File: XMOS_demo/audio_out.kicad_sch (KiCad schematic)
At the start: 26 parts, among them J5 Conn_01x06_Socket, J6 AudioJack3_SwitchT, U7 MAX97220C

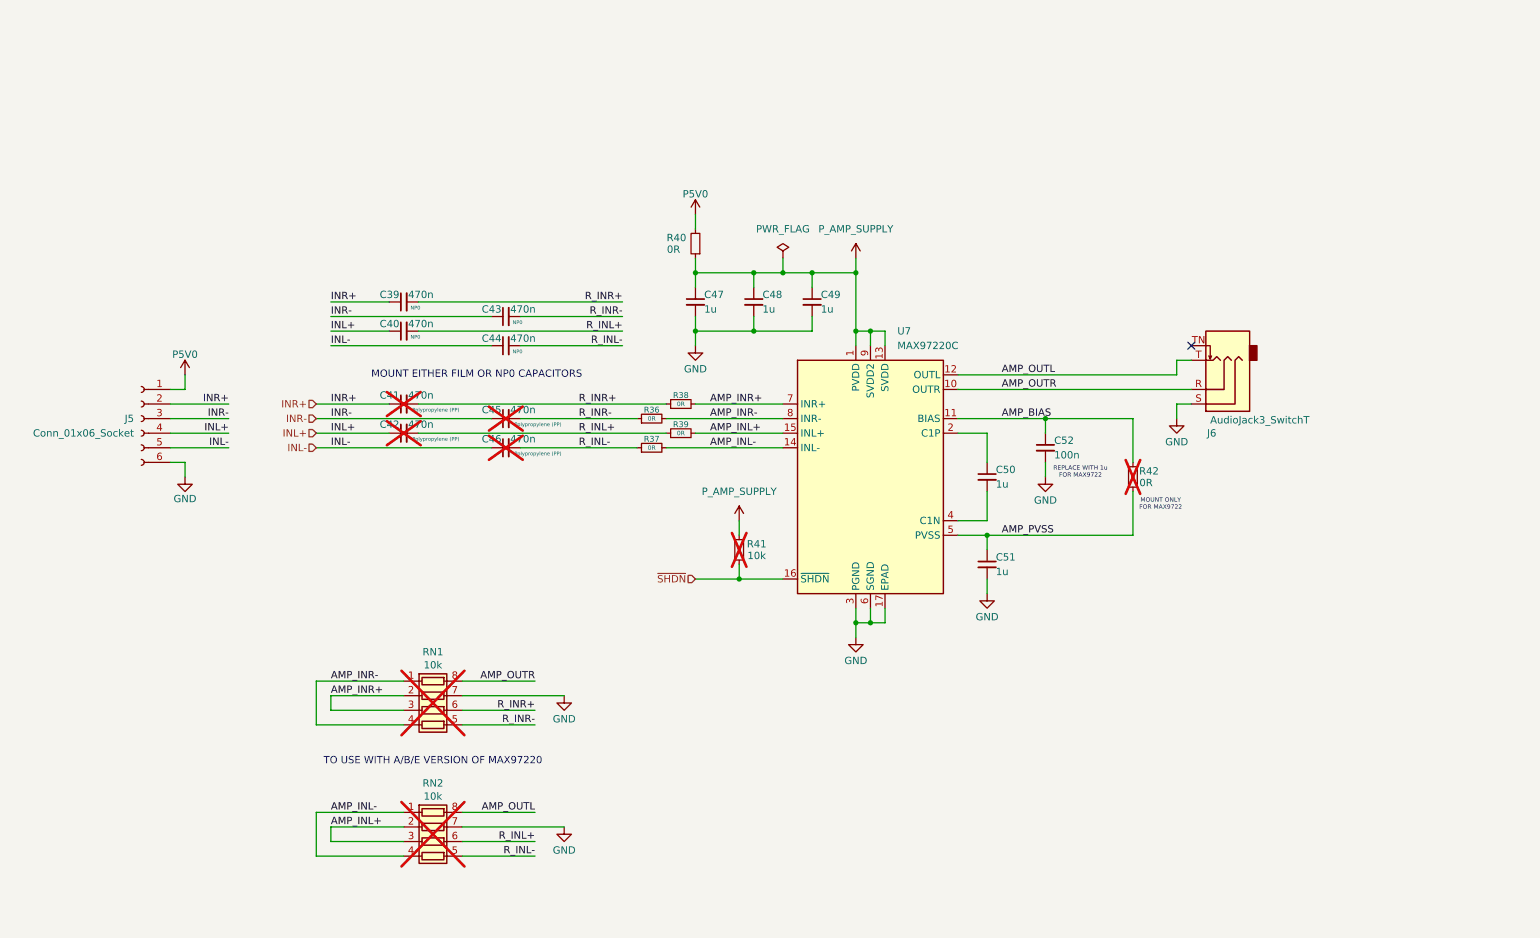
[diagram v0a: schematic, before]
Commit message: Passive lpf added to autio output
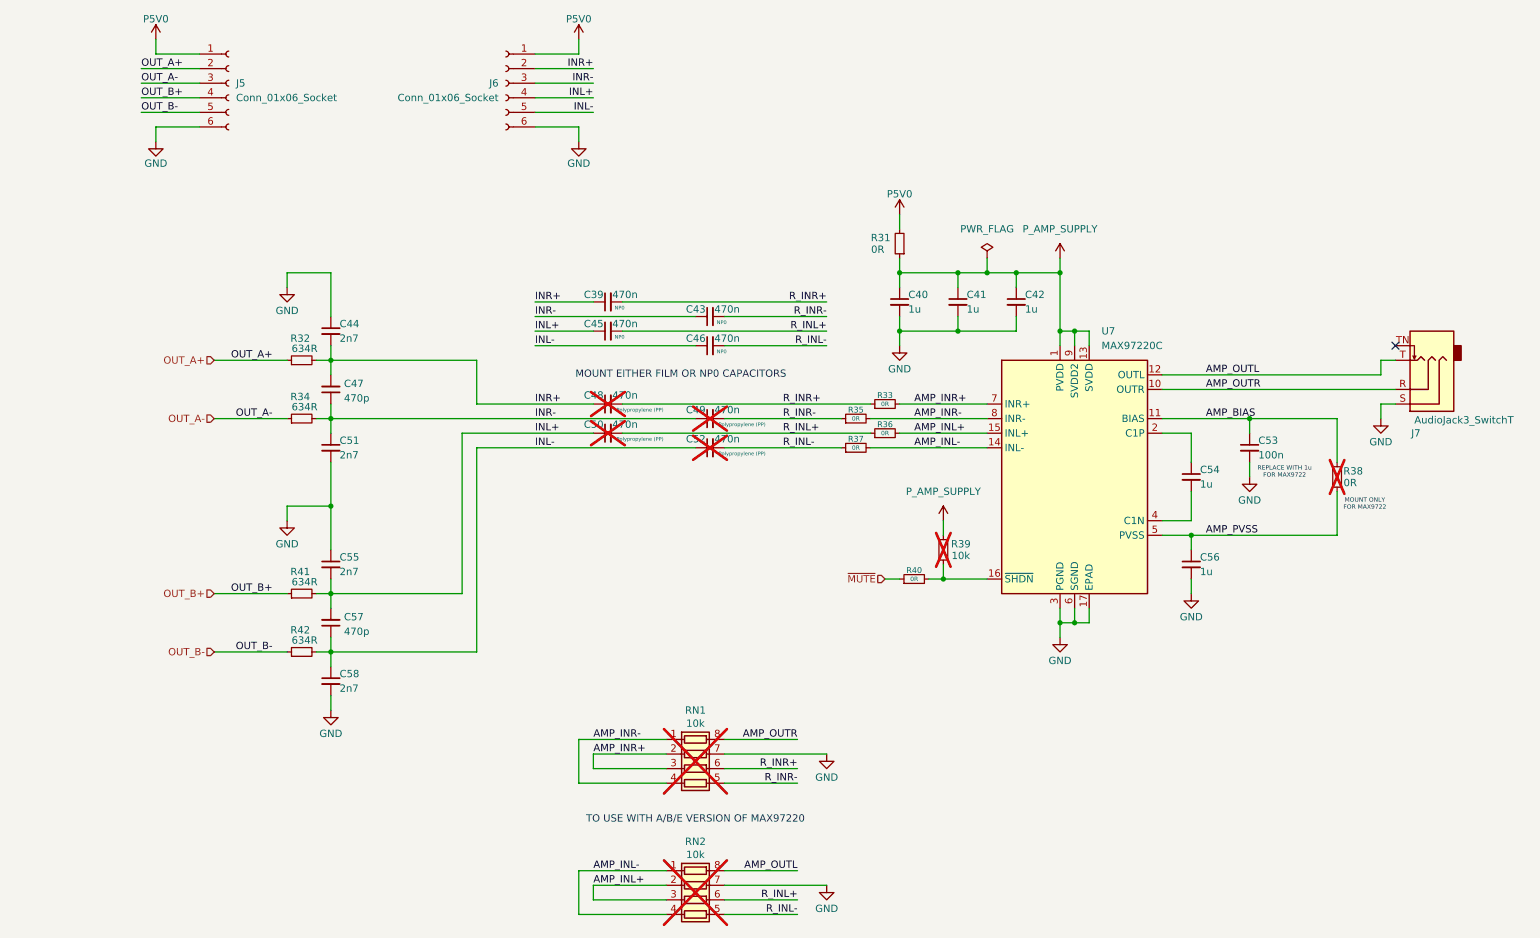
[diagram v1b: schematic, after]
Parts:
- added C44, C51, C55, C58: 2n7, Capacitor_SMD:C_0603_1608Metric, symbol Device:C_Small
- added C47, C57: 470p, Capacitor_SMD:C_0603_1608Metric, symbol Device:C_Small
- added J5: Conn_01x06_Socket, Connector_PinHeader_2.54mm:PinHeader_1x06_P2.54mm_Vertical, symbol Connector:Conn_01x06_Socket
- added R32, R34, R41, R42: 634R, Resistor_SMD:R_0603_1608Metric, symbol Device:R_Small
- added R40: 0R, Resistor_SMD:R_0603_1608Metric, symbol Device:R_Small
- renumbered C47 to C40, C48 to C41, C49 to C42, C40 to C45, C44 to C46, C41 to C48, C45 to C49, C42 to C50, C46 to C52, C52 to C53, C50 to C54, C51 to C56, J5 to J6, J6 to J7, R40 to R31, R38 to R33, R36 to R35, R39 to R36, R42 to R38, R41 to R39
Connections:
- net GND: now also C44.1, C51.2, C55.1, C58.2, J5.6 (Pin_6)
- net INL+: now also C55.2, C57.2, R41.2
- net INL-: now also C57.1, C58.1, R42.2
- net INR+: now also C44.2, C47.2, R32.2
- net INR-: now also C47.1, C51.1, R34.2
- net P5V0: now also J5.1 (Pin_1)
- net ~{SHDN}: no longer names the net of R39.2, U7.16 (~{SHDN})
- net ~{SHDN}: now also R40.2
- new net OUT_A+: J5.2 (Pin_2), R32.1
- new net OUT_A-: J5.3 (Pin_3), R34.1
- new net OUT_B+: J5.4 (Pin_4), R41.1
- new net OUT_B-: J5.5 (Pin_5), R42.1
- new net ~{MUTE}: R40.1
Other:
- moved on the sheet: C39, C40, C41, C42, C43, C45, C46, C48, C49, C50, C52, C53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

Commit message: PCB work
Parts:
- renumbered C39 to C41, C40 to C42, C41 to C43, C42 to C44, C43 to C45, C44 to C46, C45 to C47, C46 to C48, C47 to C49, C48 to C50, C49 to C51, C50 to C52, C51 to C53, C52 to C54, C53 to C55, C54 to C56, C55 to C57, C56 to C58, C57 to C59, C58 to C60
